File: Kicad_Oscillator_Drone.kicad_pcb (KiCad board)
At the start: 2 copper layers, 50.8 x 100.1 mm, 69 parts, among them J1 Power Out, J10 AudioJack, J11 AudioJack, J12 AudioJack, J14 AudioJack, J15 AudioJack, J17 AudioJack, J2 Power Out, J3 DC In Raw, J4 OSC1CV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

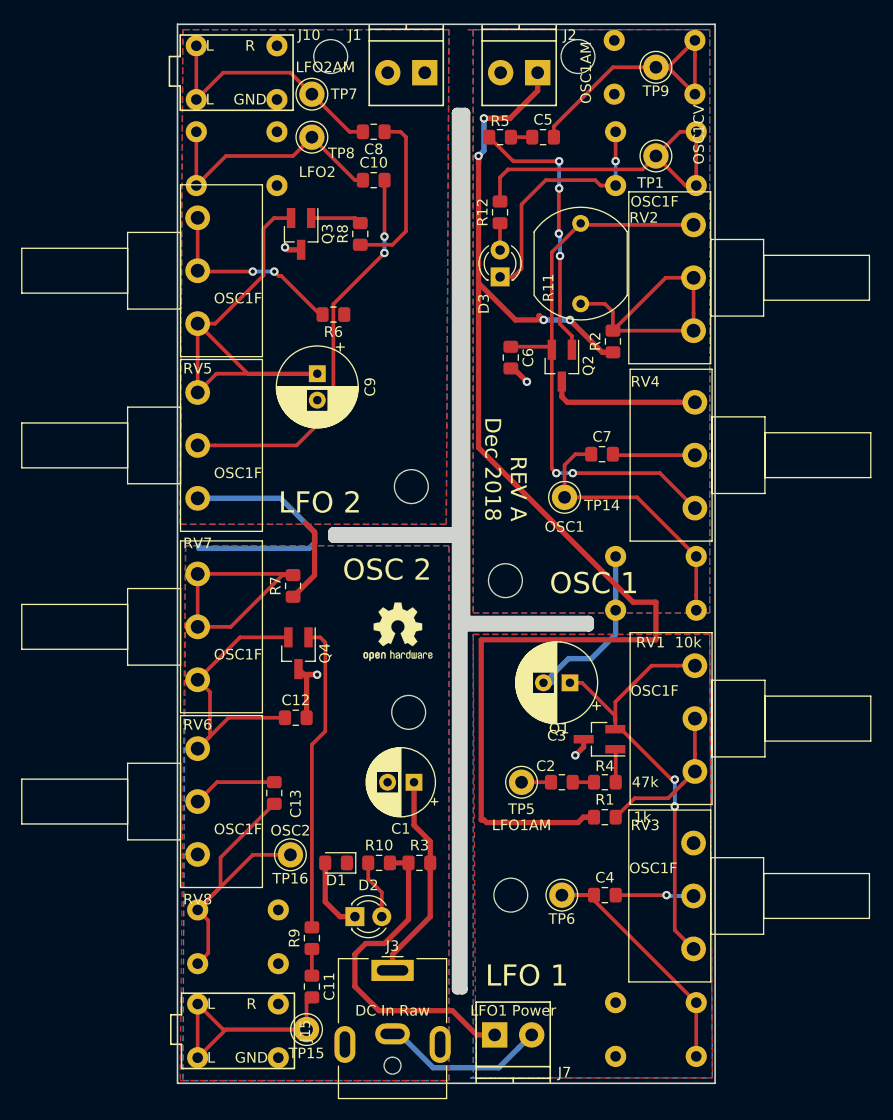
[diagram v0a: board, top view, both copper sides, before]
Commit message: Rev A2 - Text and Jack footprint update
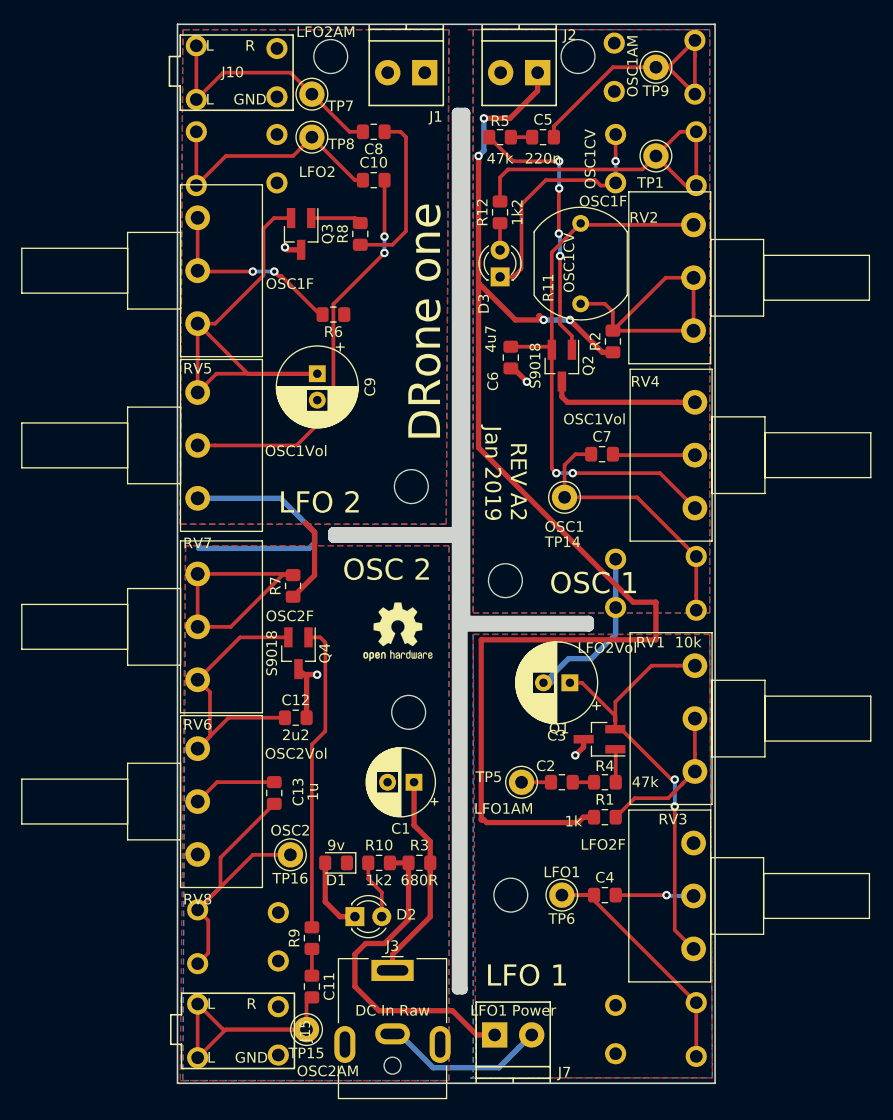
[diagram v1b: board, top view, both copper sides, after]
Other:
- board text added: "DRone one"
- board text added: "Promesoft DRone One 2019-01-21 Rev A2"
- board text added: "REV A2 Jan 2019"
- board text removed: "Promesoft DRone One 2018-12-15 Rev A"
- board text removed: "REV A Dec 2018"
